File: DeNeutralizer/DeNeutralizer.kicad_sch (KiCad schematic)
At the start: 19 parts, among them J1 Screw_Terminal_01x03, J2 Screw_Terminal_01x03, J3 Screw_Terminal_01x03, J4 Screw_Terminal_01x03, J5 Screw_Terminal_01x02, J6 Screw_Terminal_01x05, J7 Screw_Terminal_01x02, U1 PC817

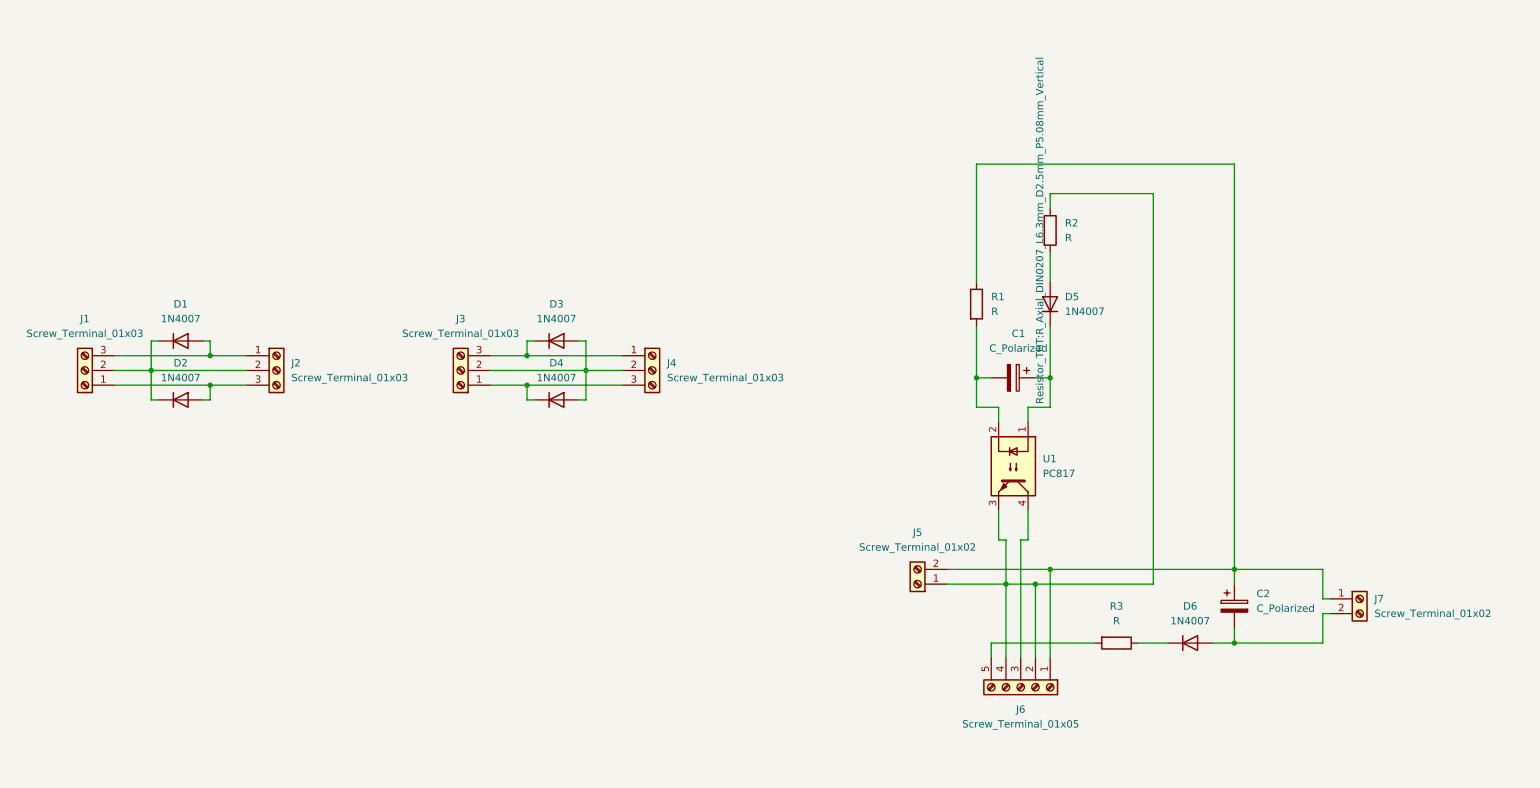
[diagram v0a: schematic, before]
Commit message: Add safety openings
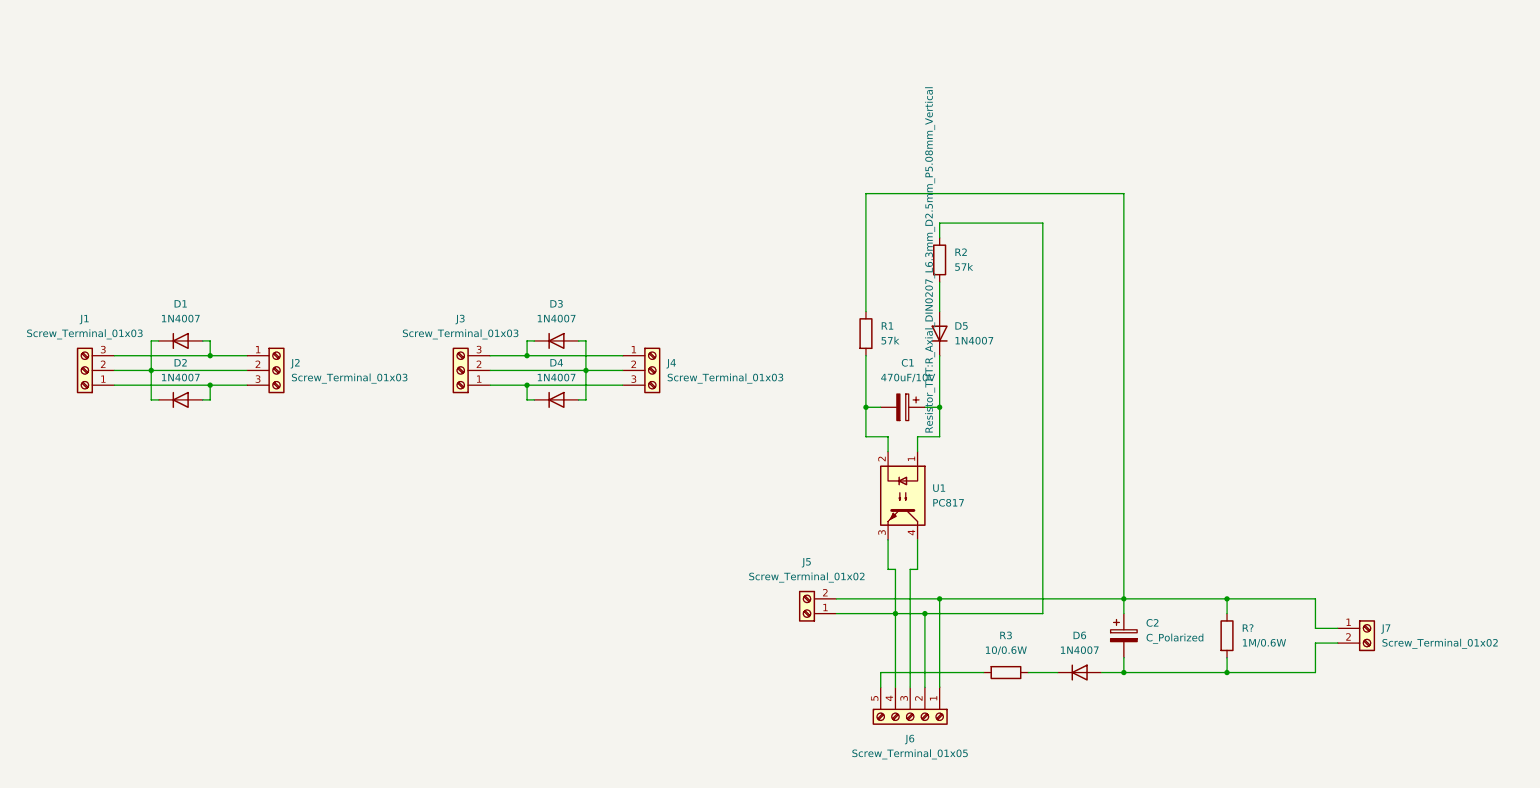
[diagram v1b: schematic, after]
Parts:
- added R?: 1M/0.6W, Resistor_THT:R_Axial_DIN0414_L11.9mm_D4.5mm_P5.08mm_Vertical, symbol Device:R
- C1: value C_Polarized -> 470uF/10V
- R1, R2: value R -> 57k
- R3: value R -> 10/0.6W
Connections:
- net at C2.1, J5.2 (Pin_2), J6.1 (Pin_1)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: now also R?.1
- net at C2.2, D6.2 (A), J7.2 (Pin_2): now also R?.2
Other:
- moved on the sheet: C1, C2, D5, D6, J5, J6, J7, R1, R2, R3, U1

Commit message: Update paths
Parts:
- gave numbers to parts that had none: 1
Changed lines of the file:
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@@
   (symbol (lib_id "Device:R") (at 232.41 132.08 0) (unit 1)
     (in_bom yes) (on_board yes) (fields_autoplaced)
-    (property "Reference" "R?" (id 0) (at 234.95 130.8099 0)
+    (property "Reference" "R4" (id 0) (at 234.95 130.8099 0)
       (effects (font (size 1.27 1.27)) (justify left))
     )
@@
     )
     (path "/834dcae7-39c3-4120-97e3-78b7973f4ba7"
-      (reference "R?") (unit 1) (value "1M/0.6W") (footprint "Resistor_THT:R_Axial_DIN0414_L11.9mm_D4.5mm_P5.08mm_Vertical")
+      (reference "R4") (unit 1) (value "1M/0.6W") (footprint "Resistor_THT:R_Axial_DIN0414_L11.9mm_D4.5mm_P5.08mm_Vertical")
     )
     (path "/4d09859b-c637-4181-bcbf-4292f51c0f42"

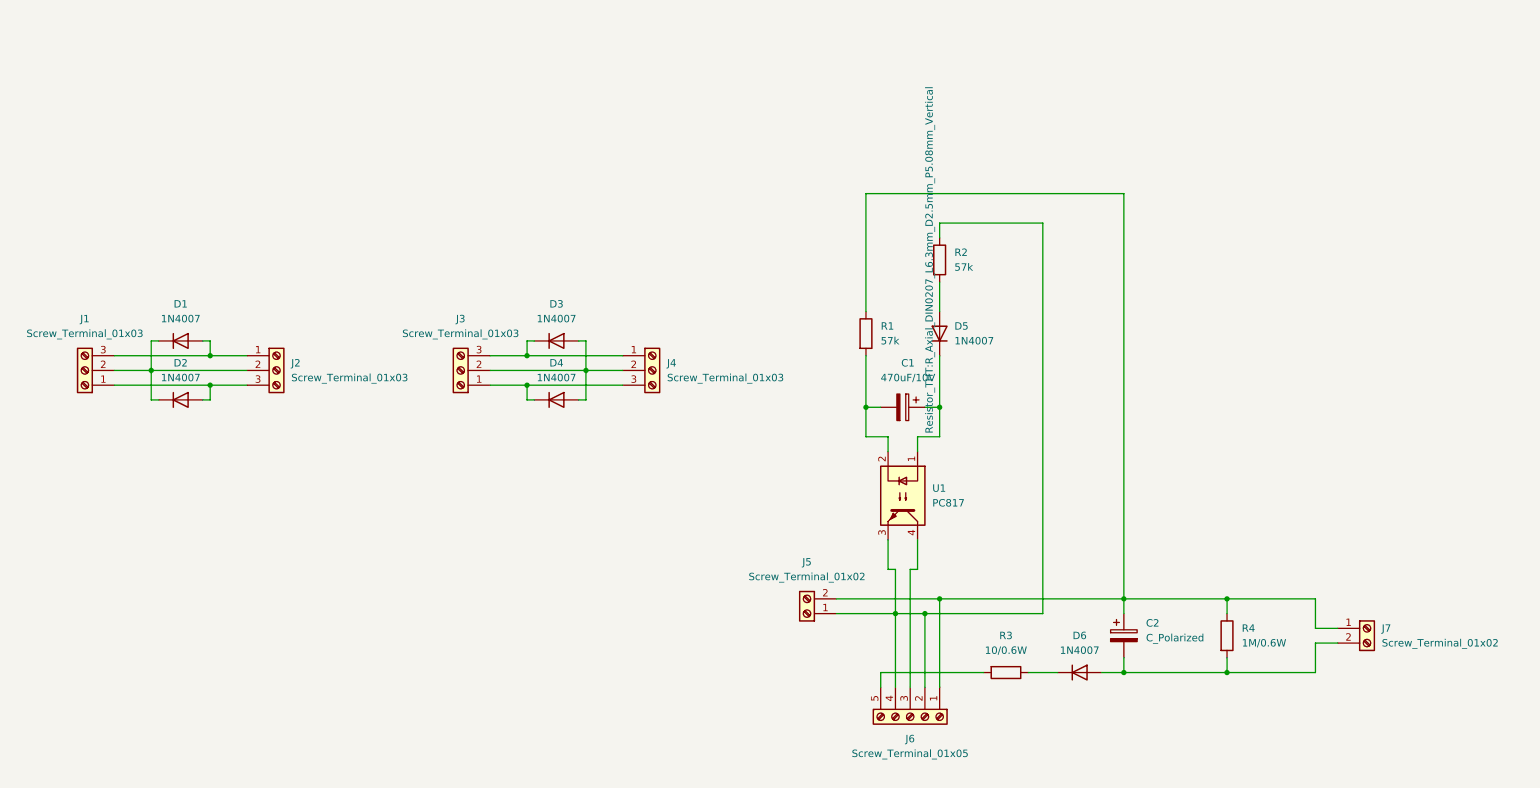
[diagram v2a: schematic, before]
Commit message: Add spark gaps
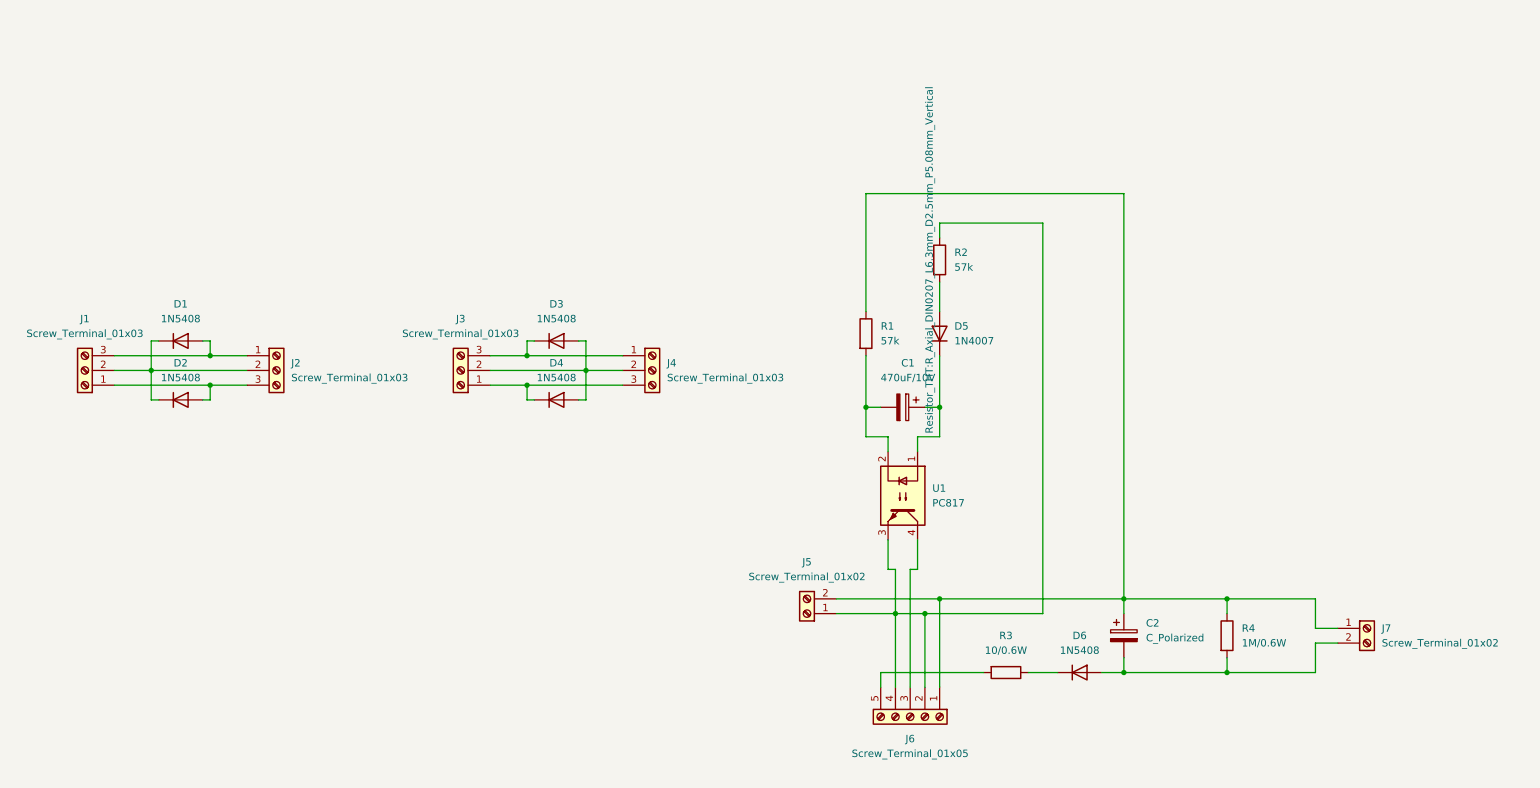
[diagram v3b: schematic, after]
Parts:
- removed D1, D2, D3, D4, D6: 1N4007, Diode_THT:D_DO-41_SOD81_P5.08mm_Vertical_KathodeUp, symbol Diode:1N4007
- added D1, D2, D3, D4, D6: 1N5408, Diode_THT:D_DO-201AD_P5.08mm_Vertical_KathodeUp, symbol Diode:1N5408
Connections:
- net at J3.3 (Pin_3), J4.1 (Pin_1): now also D3.1 (K)
- net at J3.2 (Pin_2), J4.2 (Pin_2): now also D3.2 (A), D4.2 (A)
- net at J1.2 (Pin_2), J2.2 (Pin_2): now also D1.1 (K), D2.1 (K)
- net at J1.1 (Pin_1), J2.3 (Pin_3): now also D2.2 (A)
- net at J3.1 (Pin_1), J4.3 (Pin_3): now also D4.1 (K)
- net at R3.1: now also D6.1 (K)
- net at C2.2, J7.2 (Pin_2), R4.2: now also D6.2 (A)
- net at J1.3 (Pin_3), J2.1 (Pin_1): now also D1.2 (A)
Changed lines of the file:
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@@
     (stroke (width 0) (type default) (color 0 0 0 0))
-  )
-  (symbol (lib_id "Diode:1N4007") (at 116.84 81.28 0) (unit 1)
-    (in_bom yes) (on_board yes) (fields_autoplaced)
-    (property "Reference" "D3" (id 0) (at 116.84 74.93 0))
-    (property "Value" "1N4007" (id 1) (at 116.84 77.47 0))
-    (property "Footprint" "Diode_THT:D_DO-41_SOD81_P5.08mm_Vertical_KathodeUp" (id 2) (at 116.84 85.725 0)
-      (effects (font (size 1.27 1.27)) hide)
-    )
-    (property "Datasheet" "http://www.vishay.com/docs/88503/1n4001.pdf" (id 3) (at 116.84 81.28 0)
-      (effects (font (size 1.27 1.27)) hide)
-    )
-    (pin "1")
-    (pin "2")
   )
   (symbol (lib_id "Connector:Screw_Terminal_01x05") (at 177.8 146.05 270) (unit 1)
@@
     (pin "2")
   )
-  (symbol (lib_id "Diode:1N4007") (at 52.07 91.44 0) (unit 1)
-    (in_bom yes) (on_board yes) (fields_autoplaced)
-    (property "Reference" "D2" (id 0) (at 52.07 85.09 0))
-    (property "Value" "1N4007" (id 1) (at 52.07 87.63 0))
-    (property "Footprint" "Diode_THT:D_DO-41_SOD81_P5.08mm_Vertical_KathodeUp" (id 2) (at 52.07 95.885 0)
-      (effects (font (size 1.27 1.27)) hide)
-    )
-    (property "Datasheet" "http://www.vishay.com/docs/88503/1n4001.pdf" (id 3) (at 52.07 91.44 0)
+  (symbol (lib_id "Diode:1N5408") (at 116.84 91.44 0) (unit 1)
+    (in_bom yes) (on_board yes) (fields_autoplaced)
+    (property "Reference" "D4" (id 0) (at 116.84 85.09 0))
+    (property "Value" "1N5408" (id 1) (at 116.84 87.63 0))
+    (property "Footprint" "Diode_THT:D_DO-201AD_P5.08mm_Vertical_KathodeUp" (id 2) (at 116.84 95.885 0)
+      (effects (font (size 1.27 1.27)) hide)
+    )
+    (property "Datasheet" "http://www.vishay.com/docs/88516/1n5400.pdf" (id 3) (at 116.84 91.44 0)
       (effects (font (size 1.27 1.27)) hide)
     )
@@
     (pin "2")
   )
-  (symbol (lib_id "Diode:1N4007") (at 207.01 138.43 0) (unit 1)
-    (in_bom yes) (on_board yes) (fields_autoplaced)
-    (property "Reference" "D6" (id 0) (at 207.01 132.08 0))
-    (property "Value" "1N4007" (id 1) (at 207.01 134.62 0))
-    (property "Footprint" "Diode_THT:D_DO-41_SOD81_P5.08mm_Vertical_KathodeUp" (id 2) (at 207.01 142.875 0)
-      (effects (font (size 1.27 1.27)) hide)
-    )
-    (property "Datasheet" "http://www.vishay.com/docs/88503/1n4001.pdf" (id 3) (at 207.01 138.43 0)
-      (effects (font (size 1.27 1.27)) hide)
-    )
-    (pin "1")
-    (pin "2")
-  )
   (symbol (lib_id "Isolator:PC817") (at 176.53 107.95 270) (unit 1)
     (in_bom yes) (on_board yes) (fields_autoplaced)
@@
     (pin "4")
   )
-  (symbol (lib_id "Diode:1N4007") (at 52.07 81.28 0) (unit 1)
+  (symbol (lib_id "Diode:1N5408") (at 52.07 81.28 0) (unit 1)
     (in_bom yes) (on_board yes) (fields_autoplaced)
     (property "Reference" "D1" (id 0) (at 52.07 74.93 0))
-    (property "Value" "1N4007" (id 1) (at 52.07 77.47 0))
-    (property "Footprint" "Diode_THT:D_DO-41_SOD81_P5.08mm_Vertical_KathodeUp" (id 2) (at 52.07 85.725 0)
-      (effects (font (size 1.27 1.27)) hide)
-    )
-    (property "Datasheet" "http://www.vishay.com/docs/88503/1n4001.pdf" (id 3) (at 52.07 81.28 0)
+    (property "Value" "1N5408" (id 1) (at 52.07 77.47 0))
+    (property "Footprint" "Diode_THT:D_DO-201AD_P5.08mm_Vertical_KathodeUp" (id 2) (at 52.07 85.725 0)
+      (effects (font (size 1.27 1.27)) hide)
+    )
+    (property "Datasheet" "http://www.vishay.com/docs/88516/1n5400.pdf" (id 3) (at 52.07 81.28 0)
       (effects (font (size 1.27 1.27)) hide)
     )
@@
     )
     (property "Datasheet" "http://www.vishay.com/docs/88503/1n4001.pdf" (id 3) (at 182.88 80.01 0)
-      (effects (font (size 1.27 1.27)) hide)
-    )
-    (pin "1")
-    (pin "2")
-  )
-  (symbol (lib_id "Diode:1N4007") (at 116.84 91.44 0) (unit 1)
-    (in_bom yes) (on_board yes) (fields_autoplaced)
-    (property "Reference" "D4" (id 0) (at 116.84 85.09 0))
-    (property "Value" "1N4007" (id 1) (at 116.84 87.63 0))
-    (property "Footprint" "Diode_THT:D_DO-41_SOD81_P5.08mm_Vertical_KathodeUp" (id 2) (at 116.84 95.885 0)
-      (effects (font (size 1.27 1.27)) hide)
-    )
-    (property "Datasheet" "http://www.vishay.com/docs/88503/1n4001.pdf" (id 3) (at 116.84 91.44 0)
       (effects (font (size 1.27 1.27)) hide)
     )
@@
     (pin "2")
   )
+  (symbol (lib_id "Diode:1N5408") (at 207.01 138.43 0) (unit 1)
+    (in_bom yes) (on_board yes) (fields_autoplaced)
+    (property "Reference" "D6" (id 0) (at 207.01 132.08 0))
+    (property "Value" "1N5408" (id 1) (at 207.01 134.62 0))
+    (property "Footprint" "Diode_THT:D_DO-201AD_P5.08mm_Vertical_KathodeUp" (id 2) (at 207.01 142.875 0)
+      (effects (font (size 1.27 1.27)) hide)
+    )
+    (property "Datasheet" "http://www.vishay.com/docs/88516/1n5400.pdf" (id 3) (at 207.01 138.43 0)
+      (effects (font (size 1.27 1.27)) hide)
+    )
+    (pin "1")
+    (pin "2")
+  )
+  (symbol (lib_id "Diode:1N5408") (at 116.84 81.28 0) (unit 1)
+    (in_bom yes) (on_board yes) (fields_autoplaced)
+    (property "Reference" "D3" (id 0) (at 116.84 74.93 0))
+    (property "Value" "1N5408" (id 1) (at 116.84 77.47 0))
+    (property "Footprint" "Diode_THT:D_DO-201AD_P5.08mm_Vertical_KathodeUp" (id 2) (at 116.84 85.725 0)
+      (effects (font (size 1.27 1.27)) hide)
+    )
+    (property "Datasheet" "http://www.vishay.com/docs/88516/1n5400.pdf" (id 3) (at 116.84 81.28 0)
+      (effects (font (size 1.27 1.27)) hide)
+    )
+    (pin "1")
+    (pin "2")
+  )
   (symbol (lib_id "Connector:Screw_Terminal_01x03") (at 133.35 86.36 0) (unit 1)
     (in_bom yes) (on_board yes) (fields_autoplaced)
@@
     (pin "2")
     (pin "3")
+  )
+  (symbol (lib_id "Diode:1N5408") (at 52.07 91.44 0) (unit 1)
+    (in_bom yes) (on_board yes) (fields_autoplaced)
+    (property "Reference" "D2" (id 0) (at 52.07 85.09 0))
+    (property "Value" "1N5408" (id 1) (at 52.07 87.63 0))
+    (property "Footprint" "Diode_THT:D_DO-201AD_P5.08mm_Vertical_KathodeUp" (id 2) (at 52.07 95.885 0)
+      (effects (font (size 1.27 1.27)) hide)
+    )
+    (property "Datasheet" "http://www.vishay.com/docs/88516/1n5400.pdf" (id 3) (at 52.07 91.44 0)
+      (effects (font (size 1.27 1.27)) hide)
+    )
+    (pin "1")
+    (pin "2")
   )
   (symbol (lib_id "Device:C_Polarized") (at 214.63 132.08 0) (unit 1)
@@
       (reference "C2") (unit 1) (value "C_Polarized") (footprint "Capacitor_THT:CP_Radial_D8.0mm_P5.00mm")
     )
-    (path "/561561c7-6b16-490d-a60e-232ba4099294"
-      (reference "D1") (unit 1) (value "1N4007") (footprint "Diode_THT:D_DO-41_SOD81_P5.08mm_Vertical_KathodeUp")
-    )
-    (path "/24e08573-fc55-4a33-aede-50a968ba330d"
-      (reference "D2") (unit 1) (value "1N4007") (footprint "Diode_THT:D_DO-41_SOD81_P5.08mm_Vertical_KathodeUp")
-    )
-    (path "/08628c92-cbfc-4e8c-b61b-db48e8eb72fe"
-      (reference "D3") (unit 1) (value "1N4007") (footprint "Diode_THT:D_DO-41_SOD81_P5.08mm_Vertical_KathodeUp")
-    )
-    (path "/757feaa9-5de0-4b0d-9101-fa23ac3021ad"
-      (reference "D4") (unit 1) (value "1N4007") (footprint "Diode_THT:D_DO-41_SOD81_P5.08mm_Vertical_KathodeUp")
+    (path "/58ab674c-dcf4-4aa6-be76-e3a92fc9ee3e"
+      (reference "D1") (unit 1) (value "1N5408") (footprint "Diode_THT:D_DO-201AD_P5.08mm_Vertical_KathodeUp")
+    )
+    (path "/c32ba30e-d0cc-49de-b166-db885e5dfd29"
+      (reference "D2") (unit 1) (value "1N5408") (footprint "Diode_THT:D_DO-201AD_P5.08mm_Vertical_KathodeUp")
+    )
+    (path "/8e2c7dcf-871f-4132-8035-5f6db1134f9a"
+      (reference "D3") (unit 1) (value "1N5408") (footprint "Diode_THT:D_DO-201AD_P5.08mm_Vertical_KathodeUp")
+    )
+    (path "/20a4cc9e-8570-40eb-a835-669eb7e3fcf3"
+      (reference "D4") (unit 1) (value "1N5408") (footprint "Diode_THT:D_DO-201AD_P5.08mm_Vertical_KathodeUp")
     )
     (path "/73c07c85-8041-4fbe-ab32-e3c9c0c750ce"
       (reference "D5") (unit 1) (value "1N4007") (footprint "Diode_THT:D_DO-41_SOD81_P5.08mm_Vertical_AnodeUp")
     )
-    (path "/4710300e-b23c-4e55-a49f-1555f970c4d3"
-      (reference "D6") (unit 1) (value "1N4007") (footprint "Diode_THT:D_DO-41_SOD81_P5.08mm_Vertical_KathodeUp")
+    (path "/86ae69c9-3834-40ff-9cb9-8d2dfc8c1cb2"
+      (reference "D6") (unit 1) (value "1N5408") (footprint "Diode_THT:D_DO-201AD_P5.08mm_Vertical_KathodeUp")
     )
     (path "/e2c081ba-8dcf-4b7d-8d7e-e061b463ed6a"
